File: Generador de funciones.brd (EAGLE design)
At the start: 100 x 70 mm, 41 parts, among them IC1 ICL8038, IC2 TL084P, IC3 LF353N

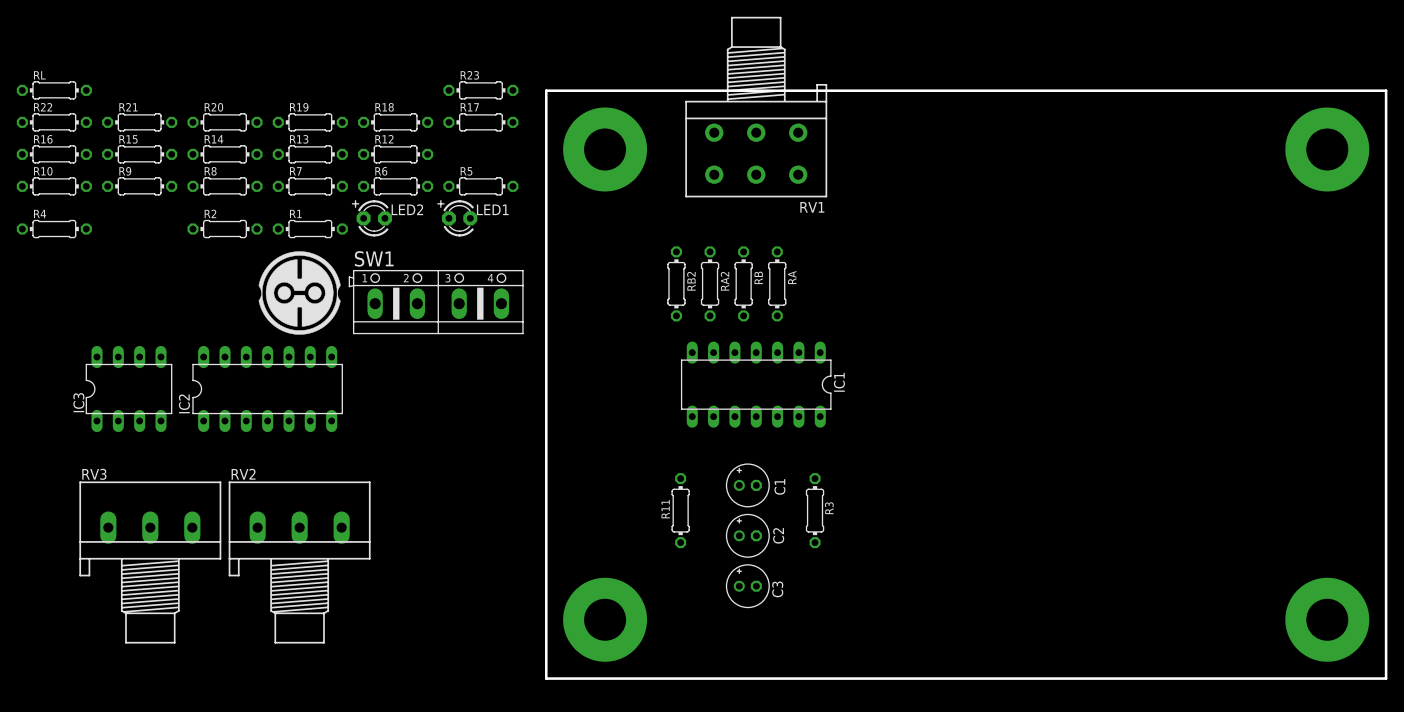
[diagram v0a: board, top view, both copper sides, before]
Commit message: Terminado Ubicacion de componentes. Inicio del ruteo
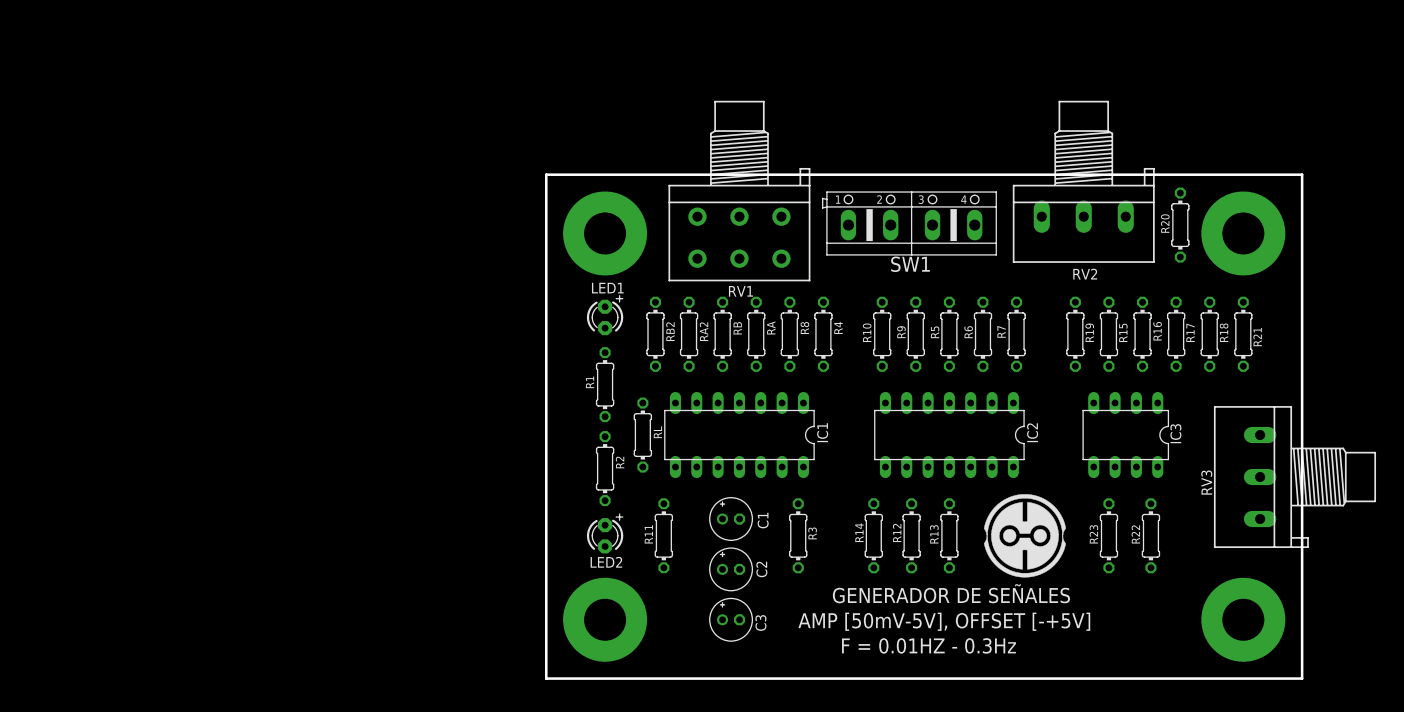
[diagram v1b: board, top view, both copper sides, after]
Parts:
- moved R22 139.6 mm to (72.0, 17.0), turned to 90 degrees
- moved R21 133.8 mm to (83.0, 41.0), turned to 90 degrees
- moved RV3 132.3 mm to (85.0, 24.0), turned to 90 degrees
- moved R16 131.3 mm to (71.0, 41.0), turned to 270 degrees
- moved IC3 118.8 mm to (69.0, 29.0), turned to 180 degrees
- moved R15 117.4 mm to (67.0, 41.0), turned to 90 degrees
- moved R20 114.4 mm to (75.5, 54.0), turned to 90 degrees
- moved RV2 100.4 mm to (64.0, 55.0), turned to 180 degrees
- moved R18 100.2 mm to (79.0, 41.0), turned to 90 degrees
- moved R10 100.1 mm to (40.0, 41.0), turned to 90 degrees
- moved R19 94.5 mm to (63.0, 41.0), turned to 90 degrees
- moved R9 94.1 mm to (44.0, 41.0), turned to 270 degrees
- moved R4 92.4 mm to (33.0, 41.0), turned to 270 degrees
- moved R23 91.7 mm to (67.0, 17.0), turned to 90 degrees
- moved U$1 91.1 mm to (57.0, 17.0)
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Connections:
- net +12V: now also LED1.A; no longer R1.2
- net GND: now also R1.1; no longer LED1.K
- net N$10: now also LED1.K, R1.2; no longer LED1.A, R1.1
- net OUT1: now also SW1.3; no longer SW1.1
- net OUT3: now also SW1.1; no longer SW1.3
- net SIN: now also R4.2; no longer R8.2
- net TRI: now also R8.2; no longer R4.2
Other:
- board size 100 x 70 mm -> 90 x 60 mm
- board text added: "AMP [50mV-5V], OFFSET [-+5V]"
- board text added: "F = 0.01HZ - 0.3Hz"
- board text added: "GENERADOR DE SEÑALES"

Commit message: Ruteo al 50%. Se esta realizando a doble capa
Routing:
- net GND: track 0.00 -> 112.8 mm
- net -12V: track 0.00 -> 74.9 mm
- net +12V: track 0.00 -> 69.5 mm
- net OUT3: track 0.00 -> 40.5 mm, vias 0 -> 1
- net N$19: track 0.00 -> 36.6 mm
- net N$24: track 0.00 -> 19.8 mm
- net N$20: track 0.00 -> 18.5 mm
- net N$2: track 0.00 -> 18.4 mm
- net N$7: track 0.00 -> 17.3 mm
- net QUAD: track 0.00 -> 14.4 mm
- net N$28: track 0.00 -> 13.7 mm
- net N$8: track 0.00 -> 13.6 mm
- net N$25: track 0.00 -> 13.6 mm
- net OFFSET: track 0.00 -> 13.2 mm
- net N$16: track 0.00 -> 12.4 mm
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
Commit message: Liberado version 1.0
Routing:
- net -12V: track 74.9 -> 146.8 mm, vias 1 -> 2
- net GND: track 112.8 -> 184.7 mm
- net +12V: track 69.5 -> 128.6 mm, vias 1 -> 2
- net OUT: track 11.5 -> 68.0 mm, vias 1 -> 2
- net N$22: track 0.00 -> 46.7 mm
- net N$27: track 0.00 -> 42.8 mm
- net OUT1: track 5.06 -> 27.5 mm
- net N$13: track 4.83 -> 27.0 mm
- net OUT2: track 4.54 -> 23.4 mm
- net N$16: track 12.4 -> 25.6 mm
- net N$21: track 9.02 -> 22.2 mm
- net N$14: track 4.62 -> 15.0 mm
- net N$26: track 0.00 -> 9.28 mm
- net N$23: track 0.00 -> 4.00 mm
- added copper zone on layer 1, net GND
- added copper zone on layer 16, net GND

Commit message: Generado imagenes SCH y BRD
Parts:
- removed U$1: LOGO_REDUCIDO, Ingenialo_logos:LOGO_10MMX10MM
- added FRAME1: A4_HORIZONTAL, Circuitos-Creativos-Estilos:LOGO
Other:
- board text added: "+12V"
- board text added: "-12V"
- board text added: "GND"
- board text added: "OUT"
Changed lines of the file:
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@@
 <layer number="16" name="Bottom" color="1" fill="1" visible="yes" active="yes"/>
 <layer number="17" name="Pads" color="2" fill="1" visible="yes" active="yes"/>
-<layer number="18" name="Vias" color="2" fill="1" visible="yes" active="yes"/>
+<layer number="18" name="Vias" color="13" fill="1" visible="yes" active="yes"/>
 <layer number="19" name="Unrouted" color="6" fill="1" visible="yes" active="yes"/>
 <layer number="20" name="Dimension" color="15" fill="1" visible="yes" active="yes"/>
-<layer number="21" name="tPlace" color="7" fill="1" visible="yes" active="yes"/>
-<layer number="22" name="bPlace" color="7" fill="1" visible="yes" active="yes"/>
+<layer number="21" name="tPlace" color="61" fill="1" visible="yes" active="yes"/>
+<layer number="22" name="bPlace" color="63" fill="1" visible="yes" active="yes"/>
 <layer number="23" name="tOrigins" color="15" fill="1" visible="yes" active="yes"/>
 <layer number="24" name="bOrigins" color="15" fill="1" visible="yes" active="yes"/>
-<layer number="25" name="tNames" color="7" fill="1" visible="yes" active="yes"/>
+<layer number="25" name="tNames" color="11" fill="1" visible="yes" active="yes"/>
 <layer number="26" name="bNames" color="7" fill="1" visible="yes" active="yes"/>
 <layer number="27" name="tValues" color="7" fill="1" visible="no" active="yes"/>
@@
 <layer number="45" name="Holes" color="7" fill="1" visible="no" active="yes"/>
 <layer number="46" name="Milling" color="3" fill="1" visible="no" active="yes"/>
-<layer number="47" name="Measures" color="7" fill="1" visible="no" active="yes"/>
+<layer number="47" name="Measures" color="24" fill="1" visible="yes" active="yes"/>
 <layer number="48" name="Document" color="7" fill="1" visible="yes" active="yes"/>
 <layer number="49" name="Reference" color="7" fill="1" visible="yes" active="yes"/>
@@
 <text x="35" y="3" size="1.778" layer="21" ratio="10">F = 0.01HZ - 0.3Hz</text>
 <text x="30" y="6" size="1.778" layer="21" ratio="10">AMP [50mV-5V], OFFSET [-+5V]</text>
+<text x="81" y="12.5" size="1.778" layer="21" ratio="10">GND</text>
+<text x="81" y="45.75" size="1.778" layer="21" ratio="10">OUT</text>
+<text x="14.25" y="4.5" size="1.778" layer="21" ratio="10" rot="R90">-12V</text>
+<text x="14.25" y="50.5" size="1.778" layer="21" ratio="10" rot="R90">+12V</text>
+<dimension x1="0" y1="60" x2="0" y2="0" x3="-5" y3="30" textsize="1.778" textratio="10" layer="47"/>
+<dimension x1="90" y1="60" x2="0" y2="60" x3="45" y3="69.5" textsize="1.778" textratio="10" layer="47"/>
 </plain>
 <attributes>
@@
 </class>
 </classes>
-<designrules name="DRC_Serigrafia_2capa">
+<designrules name="DRC_Serigrafia_2capa *">
 <description language="de">&lt;b&gt;EAGLE Design Rules&lt;/b&gt;
 &lt;p&gt;
@@
 <param name="srMaxRoundness" value="0mil"/>
 <param name="slThermalIsolate" value="20mil"/>
-<param name="slThermalsForVias" value="0"/>
+<param name="slThermalsForVias" value="1"/>
 <param name="dpMaxLengthDifference" value="10mm"/>
 <param name="dpGapFactor" value="2.5"/>
@@
 </element>
 <element name="RV1" library="pot" package="3RP/1610G" value="500k" x="23" y="55" smashed="yes" rot="R180">
-<attribute name="NAME" x="24.755" y="46.745" size="1.27" layer="25" rot="R180"/>
+<attribute name="NAME" x="24.755" y="46.745" size="1.27" layer="25" ratio="10" rot="R180"/>
 <attribute name="VALUE" x="26.555" y="45.405" size="1.27" layer="27"/>
 </element>
 <element name="RV2" library="pot" package="3RP/1610N" value="100k" x="64" y="55" smashed="yes" rot="R180">
-<attribute name="NAME" x="65.755" y="48.785" size="1.27" layer="25" rot="R180"/>
+<attribute name="NAME" x="65.755" y="48.785" size="1.27" layer="25" ratio="10" rot="R180"/>
 <attribute name="VALUE" x="71.675" y="48.96" size="1.27" layer="27" rot="R180"/>
 </element>
 <element name="RV3" library="pot" package="3RP/1610N" value="10k" x="85" y="24" smashed="yes" rot="R90">
-<attribute name="NAME" x="79.285" y="21.745" size="1.27" layer="25" rot="R90"/>
+<attribute name="NAME" x="77.715" y="25.255" size="1.27" layer="25" ratio="10" rot="R270"/>
 <attribute name="VALUE" x="78.96" y="28.325" size="1.27" layer="27" rot="R90"/>
 </element>
@@
 <attribute name="VALUE" x="33.4162" y="48.285" size="1.778" layer="27" ratio="10"/>
 </element>
-<element name="U$1" library="Ingenialo_logos" package="LOGO_10MMX10MM" value="LOGO_REDUCIDO" x="57" y="17" smashed="yes"/>
+<element name="FRAME1" library="Circuitos-Creativos-Estilos" package="LOGO" value="A4_HORIZONTAL" x="56" y="17.5"/>
 </elements>
 <signals>
